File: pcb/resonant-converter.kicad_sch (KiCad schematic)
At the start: 0 parts

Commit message: WIP: Create PCB mockup
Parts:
- added J1, J2, J3, J4: Banana_Jack_Keystone_575-8, DW-footprints:Conn_Banana_Jack_Keystone_575-8, symbol DW-connectors:Banana_Jack_Keystone_575-8
- added Q1, Q2, Q3: SIS472DN-T1-GE3, DW-footprints:PowerPAK-1212-8_Single, symbol DW-transistors:SIS472DN-T1-GE3
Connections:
- new net: Q2.1 (S), Q2.2 (S), Q2.3 (S)
- new net: Q3.1 (S), Q3.2 (S), Q3.3 (S)
- new net: Q1.1 (S), Q1.2 (S), Q1.3 (S)
- new net GND: J4.1

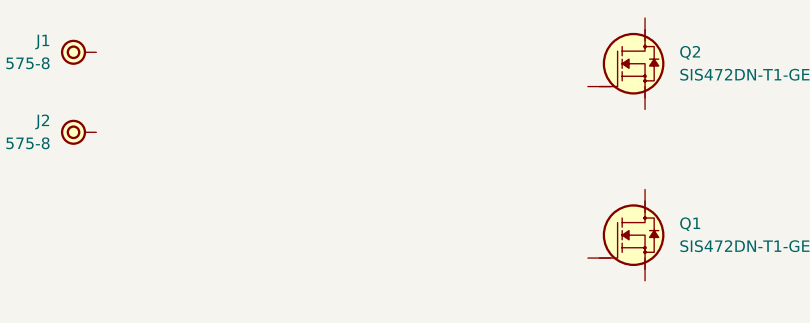
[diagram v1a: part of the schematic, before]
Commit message: Add LLC controller IC
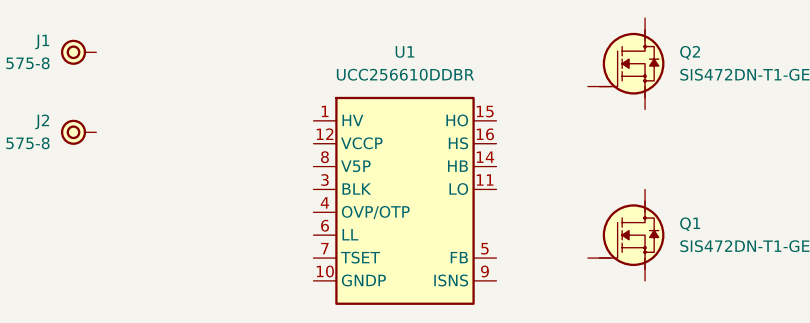
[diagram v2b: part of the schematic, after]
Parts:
- added U1: UCC256610DDBR, DW-footprints:DDB0014A, symbol DW-ICs:UCC256610DDBR
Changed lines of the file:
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@@
+	)
+	(symbol
+		(lib_id "DW-ICs:UCC256610DDBR")
+		(at 82.55 96.52 0)
+		(unit 1)
+		(exclude_from_sim no)
+		(in_bom yes)
+		(on_board yes)
+		(dnp no)
+		(fields_autoplaced yes)
+		(property "Reference" "U1"
+			(at 92.71 88.9 0)
+			(effects
+				(font
+					(size 1.27 1.27)
+					(thickness 0.15)
+				)
+			)
+		)
+		(property "Value" "UCC256610DDBR"
+			(at 110.49 99.06 0)
+			(effects
+				(font
+					(size 1.27 1.27)
+					(thickness 0.15)
+				)
+				(justify left bottom)
+				(hide yes)
+			)
+		)
+		(property "Footprint" "DW-footprints:DDB0014A"
+			(at 110.49 101.6 0)
+			(effects
+				(font
+					(size 1.27 1.27)
+					(thickness 0.15)
+				)
+				(justify left bottom)
+				(hide yes)
+			)
+		)
+		(property "Datasheet" "https://www.ti.com/lit/ds/symlink/ucc25661.pdf"
+			(at 110.49 104.14 0)
+			(effects
+				(font
+					(size 1.27 1.27)
+					(thickness 0.15)
+				)
+				(justify left bottom)
+				(hide yes)
+			)
+		)
+		(property "Description" "50kHz~750kHz LLC Power Supply Controller"
+			(at 110.49 106.68 0)
+			(effects
+				(font
+					(size 1.27 1.27)
+					(thickness 0.15)
+				)
+				(justify left bottom)
+				(hide yes)
+			)
+		)
+		(property "Manufacturer" "Texas Instruments"
+			(at 110.49 109.22 0)
+			(effects
+				(font
+					(size 1.27 1.27)
+					(thickness 0.15)
+				)
+				(justify left bottom)
+				(hide yes)
+			)
+		)
+		(property "MPN" "UCC256610DDBR"
+			(at 92.71 91.44 0)
+			(effects
+				(font
+					(size 1.27 1.27)
+					(thickness 0.15)
+				)
+			)
+		)
+		(property "LCSC" "C49247863"
+			(at 110.49 114.3 0)
+			(effects
+				(font
+					(size 1.27 1.27)
+					(thickness 0.15)
+				)
+				(justify left bottom)
+				(hide yes)
+			)
+		)
+		(pin "8"
+		)
+		(pin "9"
+		)
+		(pin "7"
+		)
+		(pin "1"
+		)
+		(pin "14"
+		)
+		(pin "16"
+		)
+		(pin "12"
+		)
+		(pin "15"
+		)
+		(pin "3"
+		)
+		(pin "4"
+		)
+		(pin "10"
+		)
+		(pin "6"
+		)
+		(pin "11"
+		)
+		(pin "5"
+		)
+		(instances
+			(project ""
+				(path "/da6185c3-cd85-4a88-bee6-2ff386eae772"
+					(reference "U1")
+					(unit 1)
+				)
+			)
+		)
 	)
 	(symbol

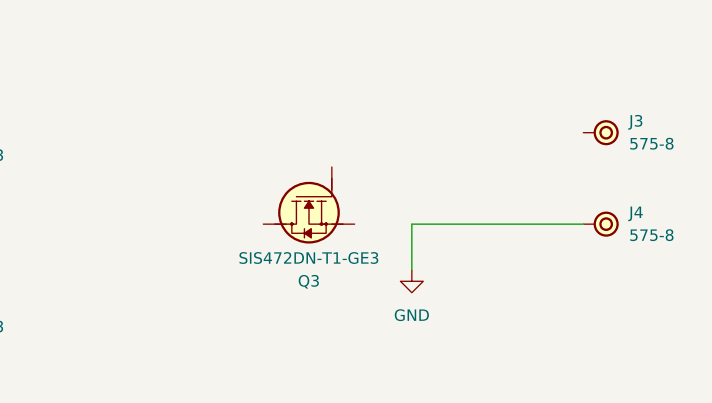
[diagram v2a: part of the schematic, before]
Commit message: Add output rectifier schottky diodes
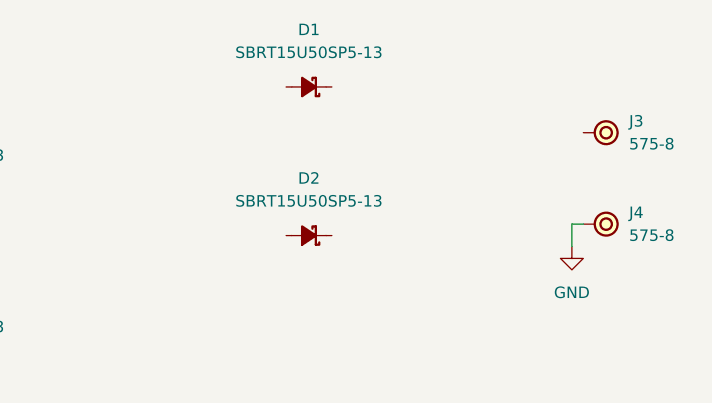
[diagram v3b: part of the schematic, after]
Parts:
- removed Q3: SIS472DN-T1-GE3, DW-footprints:PowerPAK-1212-8_Single, symbol DW-transistors:SIS472DN-T1-GE3
- added D1, D2: SBRT15U50SP5-13, DW-footprints:PowerDI-5, symbol DW-diodes:SBRT15U50SP5-13
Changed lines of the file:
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@@
 	(wire
 		(pts
-			(xy 184.15 99.06) (xy 184.15 104.14)
+			(xy 201.93 99.06) (xy 201.93 101.6)
 		)
 		(stroke
@@
 	(wire
 		(pts
-			(xy 184.15 99.06) (xy 203.2 99.06)
+			(xy 201.93 99.06) (xy 203.2 99.06)
 		)
 		(stroke
@@
 	(symbol
 		(lib_id "DW-power-symbols:GND")
-		(at 184.15 104.14 0)
+		(at 201.93 101.6 0)
 		(unit 1)
 		(exclude_from_sim no)
@@
 		(fields_autoplaced yes)
 		(property "Reference" "#PWR01"
-			(at 184.15 110.49 0)
+			(at 201.93 107.95 0)
 			(effects
 				(font
@@
 		)
 		(property "Value" "GND"
-			(at 184.15 109.22 0)
+			(at 201.93 106.68 0)
 			(effects
 				(font
@@
 		)
 		(property "Footprint" ""
-			(at 184.15 104.14 0)
+			(at 201.93 101.6 0)
 			(effects
 				(font
@@
 		)
 		(property "Datasheet" ""
-			(at 184.15 104.14 0)
+			(at 201.93 101.6 0)
 			(effects
 				(font
@@
 		)
 		(property "Description" "Power symbol creates a global label with name \"GND\" , ground"
-			(at 184.15 104.14 0)
+			(at 201.93 101.6 0)
 			(effects
 				(font
@@
 	)
 	(symbol
-		(lib_id "DW-transistors:SIS472DN-T1-GE3")
-		(at 175.26 92.71 90)
-		(mirror x)
+		(lib_id "DW-diodes:SBRT15U50SP5-13")
+		(at 175.26 83.82 180)
 		(unit 1)
 		(exclude_from_sim no)
@@
 		(on_board yes)
 		(dnp no)
-		(property "Reference" "Q3"
-			(at 172.72 105.41 90)
-			(effects
-				(font
-					(size 1.27 1.27)
-					(thickness 0.15)
-				)
-			)
-		)
-		(property "Value" "SIS472DN-T1-GE3"
-			(at 177.8 102.87 0)
-			(effects
-				(font
-					(size 1.27 1.27)
-					(thickness 0.15)
-				)
-				(justify left bottom)
-				(hide yes)
-			)
-		)
-		(property "Footprint" "DW-footprints:PowerPAK-1212-8_Single"
-			(at 180.34 102.87 0)
-			(effects
-				(font
-					(size 1.27 1.27)
-					(thickness 0.15)
-				)
-				(justify left bottom)
-				(hide yes)
-			)
-		)
-		(property "Datasheet" "https://www.lcsc.com/datasheet/C727441.pdf"
-			(at 182.88 102.87 0)
-			(effects
-				(font
-					(size 1.27 1.27)
-					(thickness 0.15)
-				)
-				(justify left bottom)
-				(hide yes)
-			)
-		)
-		(property "Description" "30V 8.9mΩ@10V,15A 2.5V 1 N-Channel PowerPAK1212-8 MOSFETs ROHS"
-			(at 185.42 102.87 0)
-			(effects
-				(font
-					(size 1.27 1.27)
-					(thickness 0.15)
-				)
-				(justify left bottom)
-				(hide yes)
-			)
-		)
-		(property "Manufacturer" "VISHAY"
-			(at 187.96 102.87 0)
-			(effects
-				(font
-					(size 1.27 1.27)
-					(thickness 0.15)
-				)
-				(justify left bottom)
-				(hide yes)
-			)
-		)
-		(property "MPN" "SIS472DN-T1-GE3"
-			(at 172.72 102.87 90)
-			(effects
-				(font
-					(size 1.27 1.27)
-					(thickness 0.15)
-				)
-			)
-		)
-		(property "LCSC" "C727441"
-			(at 193.04 102.87 0)
-			(effects
-				(font
-					(size 1.27 1.27)
-					(thickness 0.15)
-				)
-				(justify left bottom)
-				(hide yes)
-			)
-		)
-		(property "Id" "20A"
-			(at 195.58 102.87 0)
-			(effects
-				(font
-					(size 1.27 1.27)
-					(thickness 0.15)
-				)
-				(justify left bottom)
-				(hide yes)
-			)
-		)
-		(property "Vds" "30V"
-			(at 198.12 102.87 0)
-			(effects
-				(font
-					(size 1.27 1.27)
-					(thickness 0.15)
-				)
-				(justify left bottom)
-				(hide yes)
-			)
-		)
-		(property "Vgs" "20V"
-			(at 200.66 102.87 0)
-			(effects
-				(font
-					(size 1.27 1.27)
-					(thickness 0.15)
-				)
-				(justify left bottom)
-				(hide yes)
-			)
-		)
-		(property "Rds(on)" "8.9mΩ"
-			(at 203.2 102.87 0)
-			(effects
-				(font
-					(size 1.27 1.27)
-					(thickness 0.15)
-				)
-				(justify left bottom)
-				(hide yes)
-			)
-		)
-		(pin "4"
-		)
-		(pin "3"
+		(fields_autoplaced yes)
+		(property "Reference" "D1"
+			(at 172.72 77.47 0)
+			(effects
+				(font
+					(size 1.27 1.27)
+					(thickness 0.15)
+				)
+			)
+		)
+		(property "Value" "SBRT15U50SP5-13"
+			(at 162.56 81.28 0)
+			(effects
+				(font
+					(size 1.27 1.27)
+					(thickness 0.15)
+				)
+				(justify left bottom)
+				(hide yes)
+			)
+		)
+		(property "Footprint" "DW-footprints:PowerDI-5"
+			(at 162.56 78.74 0)
+			(effects
+				(font
+					(size 1.27 1.27)
+					(thickness 0.15)
+				)
+				(justify left bottom)
+				(hide yes)
+			)
+		)
+		(property "Datasheet" "https://www.lcsc.com/datasheet/C211388.pdf"
+			(at 162.56 76.2 0)
+			(effects
+				(font
+					(size 1.27 1.27)
+					(thickness 0.15)
+				)
+				(justify left bottom)
+				(hide yes)
+			)
+		)
+		(property "Description" "50V 410mV@15A 15A PowerDI-5 Single Schottky Diode"
+			(at 162.56 73.66 0)
+			(effects
+				(font
+					(size 1.27 1.27)
+					(thickness 0.15)
+				)
+				(justify left bottom)
+				(hide yes)
+			)
+		)
+		(property "Manufacturer" "DIODES"
+			(at 162.56 71.12 0)
+			(effects
+				(font
+					(size 1.27 1.27)
+					(thickness 0.15)
+				)
+				(justify left bottom)
+				(hide yes)
+			)
+		)
+		(property "MPN" "SBRT15U50SP5-13"
+			(at 172.72 80.01 0)
+			(effects
+				(font
+					(size 1.27 1.27)
+					(thickness 0.15)
+				)
+			)
+		)
+		(property "LCSC" "C211388"
+			(at 162.56 66.04 0)
+			(effects
+				(font
+					(size 1.27 1.27)
+					(thickness 0.15)
+				)
+				(justify left bottom)
+				(hide yes)
+			)
+		)
+		(property "Reverse Voltage" "50V"
+			(at 162.56 63.5 0)
+			(effects
+				(font
+					(size 1.27 1.27)
+					(thickness 0.15)
+				)
+				(justify left bottom)
+				(hide yes)
+			)
+		)
+		(property "Continuous Forward Current" "15A"
+			(at 162.56 60.96 0)
+			(effects
+				(font
+					(size 1.27 1.27)
+					(thickness 0.15)
+				)
+				(justify left bottom)
+				(hide yes)
+			)
+		)
+		(pin "1"
 		)
 		(pin "2"
 		)
+		(instances
+			(project ""
+				(path "/da6185c3-cd85-4a88-bee6-2ff386eae772"
+					(reference "D1")
+					(unit 1)
+				)
+			)
+		)
+	)
+	(symbol
+		(lib_id "DW-diodes:SBRT15U50SP5-13")
+		(at 175.26 100.33 180)
+		(unit 1)
+		(exclude_from_sim no)
+		(in_bom yes)
+		(on_board yes)
+		(dnp no)
+		(fields_autoplaced yes)
+		(property "Reference" "D2"
+			(at 172.72 93.98 0)
+			(effects
+				(font
+					(size 1.27 1.27)
+					(thickness 0.15)
+				)
+			)
+		)
+		(property "Value" "SBRT15U50SP5-13"
+			(at 162.56 97.79 0)
+			(effects
+				(font
+					(size 1.27 1.27)
+					(thickness 0.15)
+				)
+				(justify left bottom)
+				(hide yes)
+			)
+		)
+		(property "Footprint" "DW-footprints:PowerDI-5"
+			(at 162.56 95.25 0)
+			(effects
+				(font
+					(size 1.27 1.27)
+					(thickness 0.15)
+				)
+				(justify left bottom)
+				(hide yes)
+			)
+		)
+		(property "Datasheet" "https://www.lcsc.com/datasheet/C211388.pdf"
+			(at 162.56 92.71 0)
+			(effects
+				(font
+					(size 1.27 1.27)
+					(thickness 0.15)
+				)
+				(justify left bottom)
+				(hide yes)
+			)
+		)
+		(property "Description" "50V 410mV@15A 15A PowerDI-5 Single Schottky Diode"
+			(at 162.56 90.17 0)
+			(effects
+				(font
+					(size 1.27 1.27)
+					(thickness 0.15)
+				)
+				(justify left bottom)
+				(hide yes)
+			)
+		)
+		(property "Manufacturer" "DIODES"
+			(at 162.56 87.63 0)
+			(effects
+				(font
+					(size 1.27 1.27)
+					(thickness 0.15)
+				)
+				(justify left bottom)
+				(hide yes)
+			)
+		)
+		(property "MPN" "SBRT15U50SP5-13"
+			(at 172.72 96.52 0)
+			(effects
+				(font
+					(size 1.27 1.27)
+					(thickness 0.15)
+				)
+			)
+		)
+		(property "LCSC" "C211388"
+			(at 162.56 82.55 0)
+			(effects
+				(font
+					(size 1.27 1.27)
+					(thickness 0.15)
+				)
+				(justify left bottom)
+				(hide yes)
+			)
+		)
+		(property "Reverse Voltage" "50V"
+			(at 162.56 80.01 0)
+			(effects
+				(font
+					(size 1.27 1.27)
+					(thickness 0.15)
+				)
+				(justify left bottom)
+				(hide yes)
+			)
+		)
+		(property "Continuous Forward Current" "15A"
+			(at 162.56 77.47 0)
+			(effects
+				(font
+					(size 1.27 1.27)
+					(thickness 0.15)
+				)
+				(justify left bottom)
+				(hide yes)
+			)
+		)
 		(pin "1"
 		)
-		(pin "5"
+		(pin "2"
 		)
 		(instances
 			(project "resonant-converter"
 				(path "/da6185c3-cd85-4a88-bee6-2ff386eae772"
-					(reference "Q3")
+					(reference "D2")
 					(unit 1)
 				)

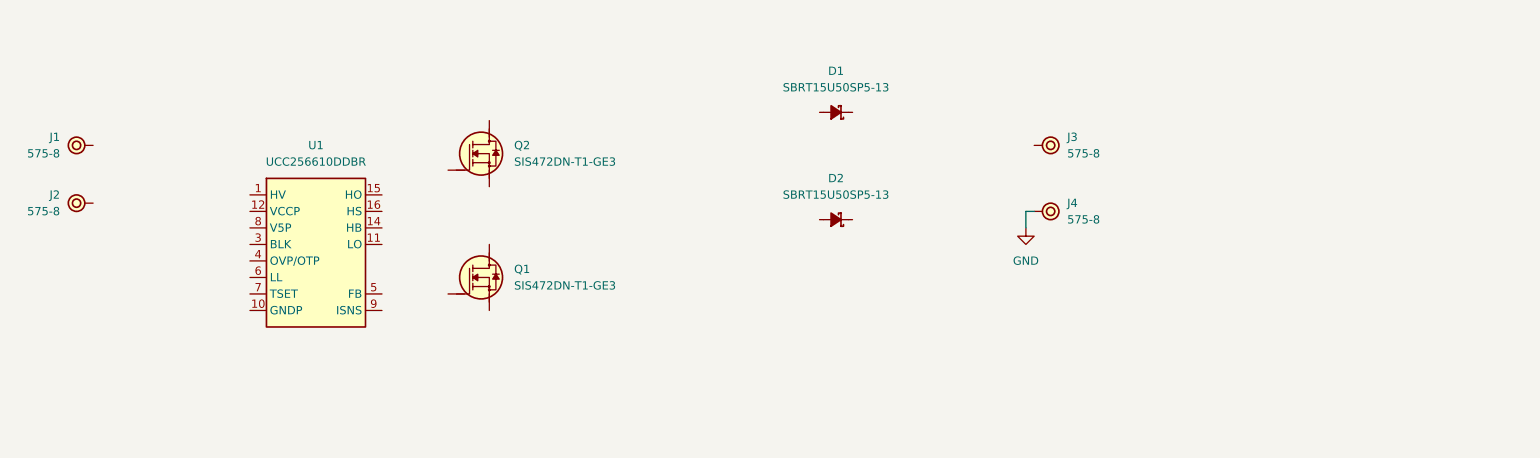
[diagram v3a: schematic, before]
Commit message: Add synchronous rectifier
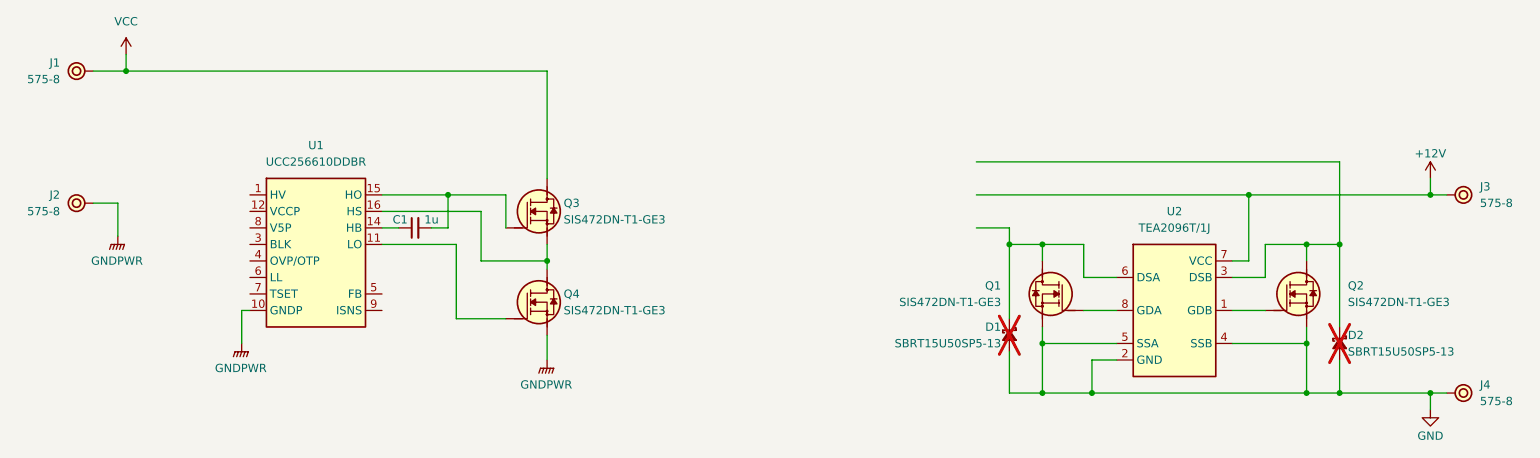
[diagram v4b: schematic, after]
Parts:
- added C1: C-1u-0402, DW-footprints:C_0402_1005Metric, symbol DW-capacitors:C-1u-0402
- added Q3, Q4: SIS472DN-T1-GE3, DW-footprints:PowerPAK-1212-8_Single, symbol DW-transistors:SIS472DN-T1-GE3
- added U2: TEA2096T/1J, DW-footprints:SOIC-8_3.9x4.9mm_P1.27mm, symbol DW-ICs:TEA2096T/1J
- D1, D2: now not fitted
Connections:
- net GND: now also D1.2 (A), D2.2 (A), Q1.1 (S), Q1.2 (S), Q1.3 (S), Q2.1 (S), Q2.2 (S), Q2.3 (S), U2.2 (GND), U2.4 (SSB), U2.5 (SSA)
- net at Q2.4 (G): now also U2.1 (GDB)
- net at Q2.5 (D): now also D2.1 (C), U2.3 (DSB)
- net +12V: now reaches J3.1
- net +12V: now also U2.7 (VCC)
- net GNDPWR: now reaches U1.10 (GNDP)
- net GNDPWR: now also J2.1, Q4.1 (S), Q4.2 (S), Q4.3 (S)
- net at U1.11 (LO): now also Q4.4 (G)
- net at U1.14 (HB): now also C1.1
- net at U1.15 (HO): now also C1.2, Q3.4 (G)
- net at U1.16 (HS): now also Q3.1 (S), Q3.2 (S), Q3.3 (S), Q4.5 (D)
- net at D1.1 (C): now also Q1.5 (D), U2.6 (DSA)
- net VCC: now reaches J1.1
- net VCC: now also Q3.5 (D)
- net at Q1.4 (G): now also U2.8 (GDA)
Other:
- moved on the sheet: J1, J3, J4, Q1, Q2

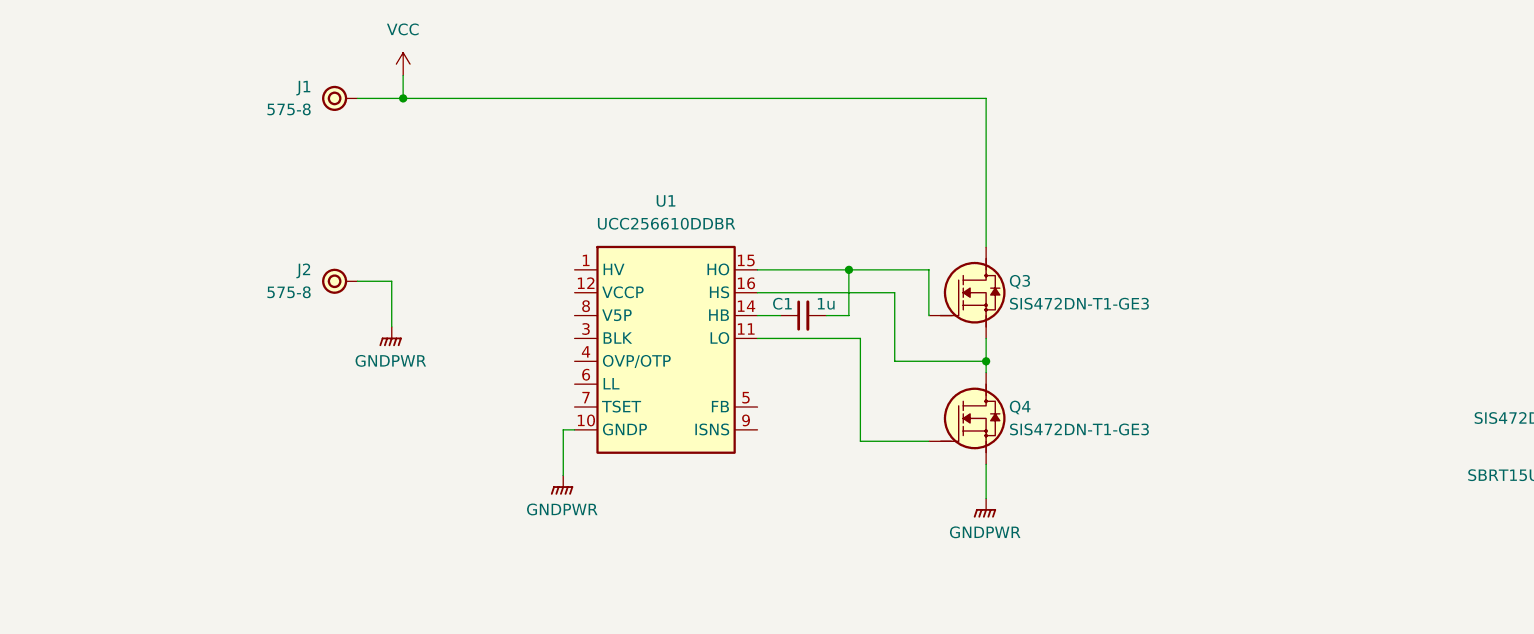
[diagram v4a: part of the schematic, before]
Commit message: Add resonant inductor and capacitors
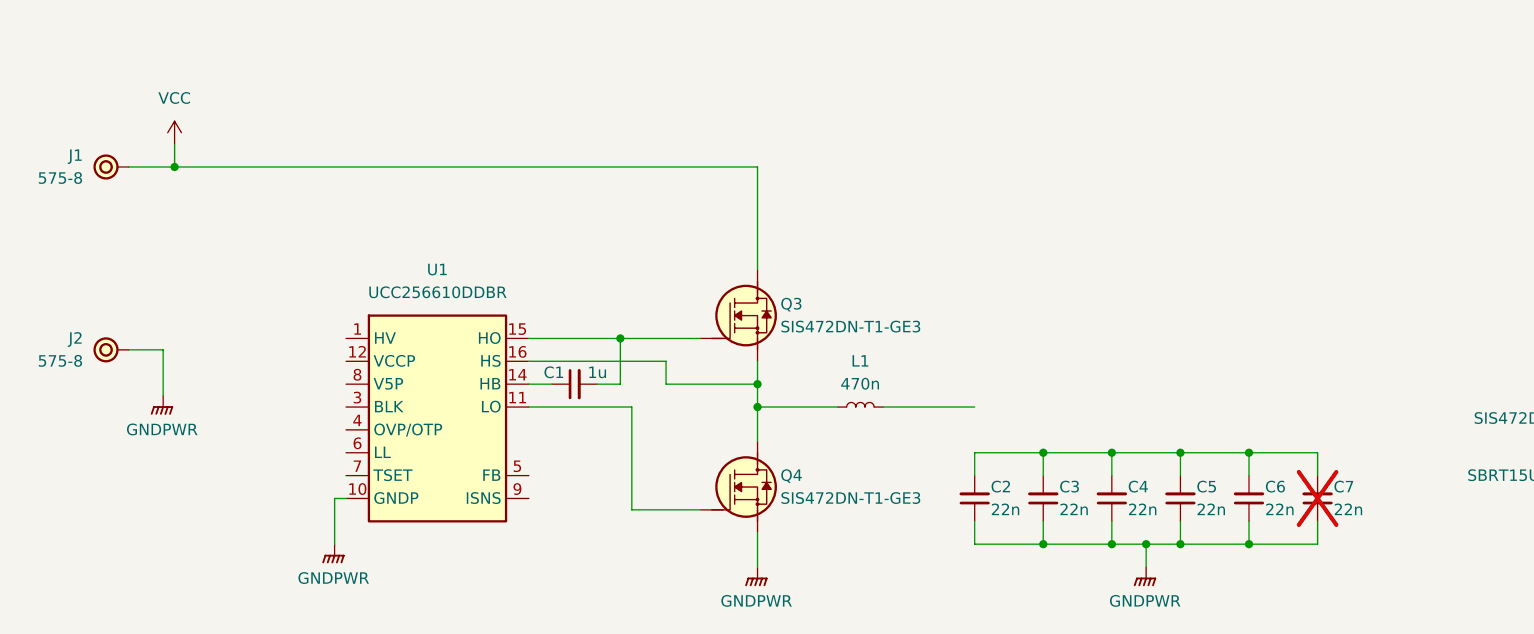
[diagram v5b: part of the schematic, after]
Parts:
- added C2, C3, C4, C5, C6, C7: C-22n-100V-C0G-1206, DW-footprints:C_1206_3216Metric, symbol DW-capacitors:C-22n-100V-C0G-1206
- added L1: L-470n-7A-dehongganying-DH0520H-R47M, DW-footprints:L-dehongganying-DH0520H, symbol DW-inductors:L-470n-7A-dehongganying-DH0520H-R47M
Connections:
- net GNDPWR: now also C2.1, C3.1, C4.1, C5.1, C6.1, C7.1
- net at Q3.1 (S), Q3.2 (S), Q3.3 (S)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: now also L1.1
- new net: C2.2, C3.2, C4.2, C5.2, C6.2, C7.2
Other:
- moved on the sheet: C1, J1, J2, Q3, Q4, U1
